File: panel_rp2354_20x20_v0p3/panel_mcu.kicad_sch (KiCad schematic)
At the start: 33 parts, among them SW1 SW_Push, SW2 SW_Push, U1 APS6404L-3SQR, U2 RP2354B_80QFN, Y1 ABM8-272-T3

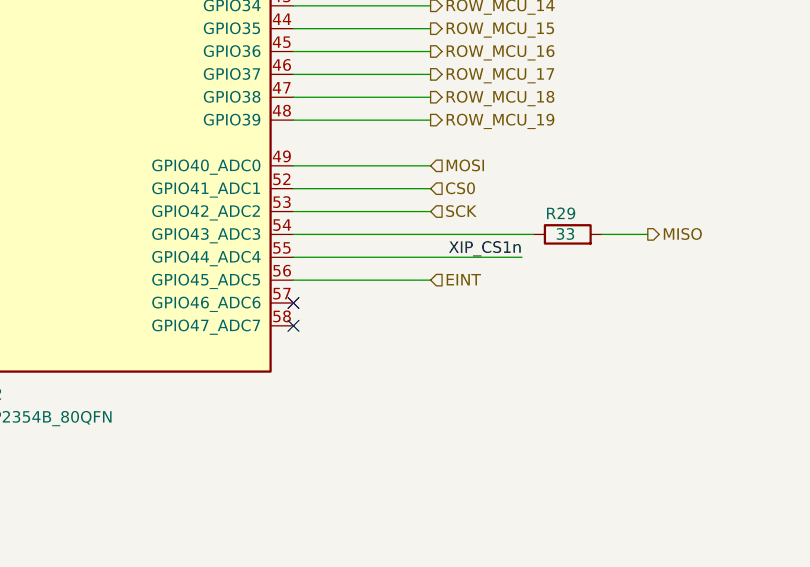
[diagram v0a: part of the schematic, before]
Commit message: fix XIP_CS1n pind
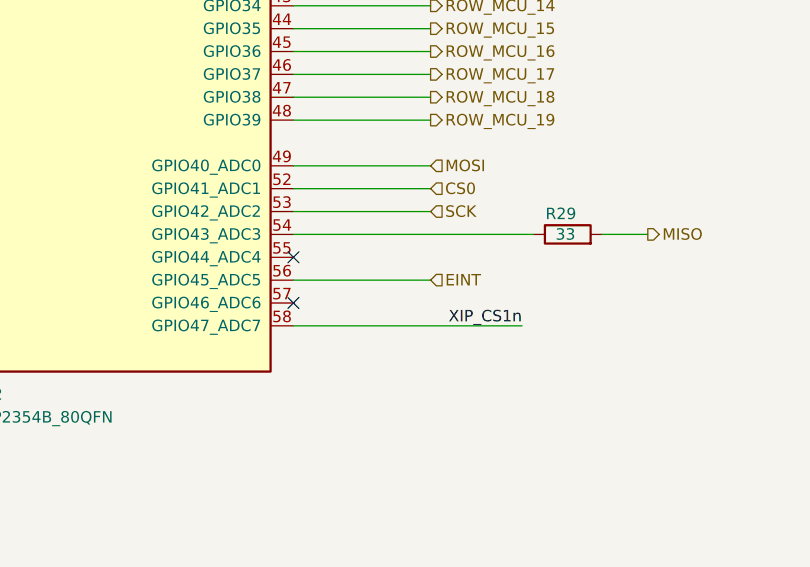
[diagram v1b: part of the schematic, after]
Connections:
- net XIP_CS1n: now also U2.58 (GPIO47_ADC7); no longer U2.55 (GPIO44_ADC4)
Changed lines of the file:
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@@
 		(title "G6 panel 45mm RP2354")
 		(date "2026-04-09")
-		(rev "v0.3.0")
+		(rev "v0.3.1")
 		(company "IORodeo for Reiserlab @ Janelia")
 	)
@@
 	)
 	(no_connect
-		(at 241.3 204.47)
+		(at 241.3 196.85)
 	)
 	(no_connect
@@
 	(wire
 		(pts
-			(xy 241.3 196.85) (xy 266.7 196.85)
+			(xy 241.3 204.47) (xy 266.7 204.47)
 		)
 		(stroke
@@
 	)
 	(label "XIP_CS1n"
-		(at 266.7 196.85 180)
+		(at 266.7 204.47 180)
 		(effects
 			(font
